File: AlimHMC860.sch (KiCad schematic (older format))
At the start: 21 parts, among them U2 HMC860LP3E

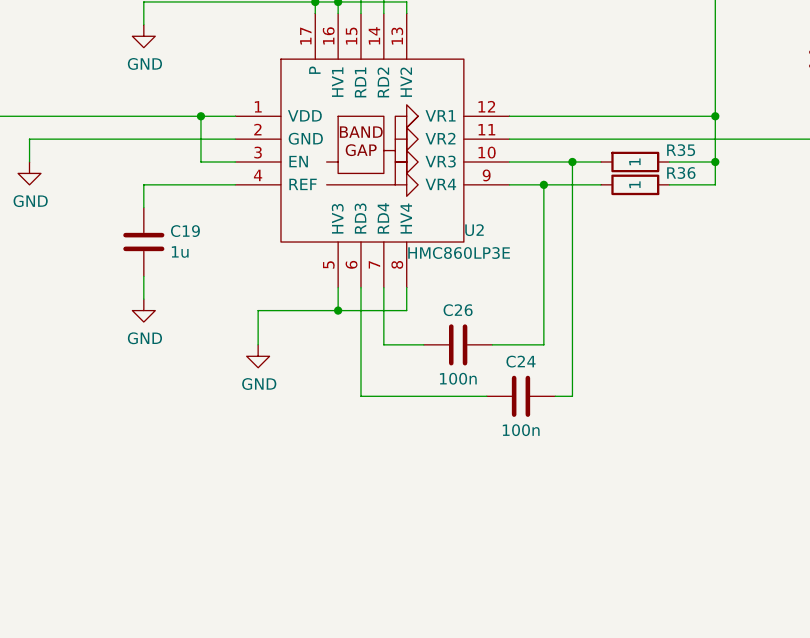
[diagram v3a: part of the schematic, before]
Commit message: added the option to switch HMC860 for HMC1060
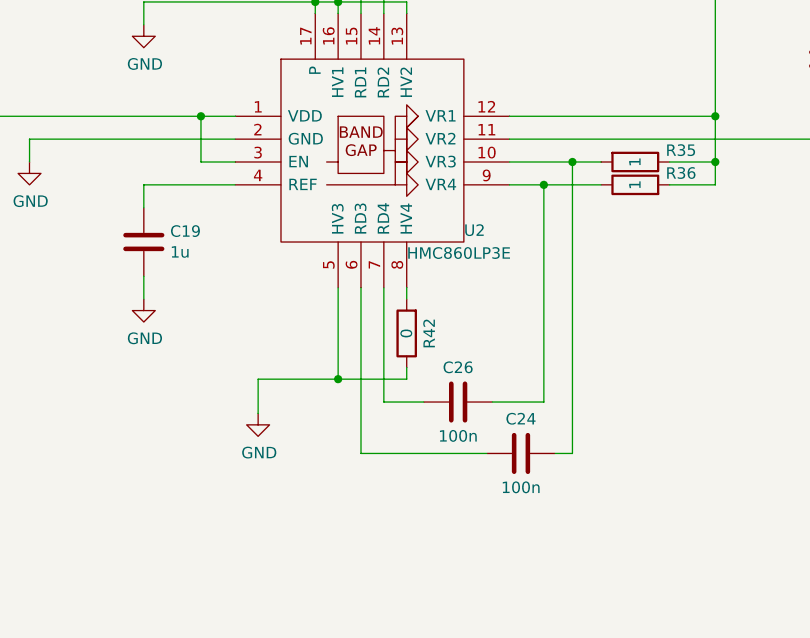
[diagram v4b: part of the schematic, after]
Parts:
- added R42: 0, Resistor_SMD:R_0603_1608Metric_Pad0.98x0.95mm_HandSolder, symbol Device:R
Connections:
- net GND: now also R42.1; no longer U2.8 (HV4)
- new net: R42.2, U2.8 (HV4)
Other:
- moved on the sheet: C24, C26
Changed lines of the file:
@@
 L Device:C C?
 U 1 1 618A0679
-P 5375 4000
+P 5375 4250
 AR Path="/618A0679" Ref="C?"  Part="1"
 AR Path="/6188E6DD/618A0679" Ref="C26"  Part="1"
-F 0 "C26" V 5225 4000 50  0000 C CNN
-F 1 "100n" V 5525 4000 50  0000 C CNN
-F 2 "Capacitor_SMD:C_0603_1608Metric_Pad1.08x0.95mm_HandSolder" H 5413 3850 50  0001 C CNN
-F 3 "~" H 5375 4000 50  0001 C CNN
-	1    5375 4000
-	0    1    1    0
-$EndComp
-Wire Wire Line
-	5525 4000 5750 4000
+F 0 "C26" V 5225 4250 50  0000 C CNN
+F 1 "100n" V 5525 4250 50  0000 C CNN
+F 2 "Capacitor_SMD:C_0603_1608Metric_Pad1.08x0.95mm_HandSolder" H 5413 4100 50  0001 C CNN
+F 3 "~" H 5375 4250 50  0001 C CNN
+	1    5375 4250
+	0    1    1    0
+$EndComp
+Wire Wire Line
+	5525 4250 5750 4250
 $Comp
 L Device:C C?
@@
 L Device:C C?
 U 1 1 618FCC1B
-P 5650 4225
+P 5650 4475
 AR Path="/618FCC1B" Ref="C?"  Part="1"
 AR Path="/6188E6DD/618FCC1B" Ref="C24"  Part="1"
-F 0 "C24" V 5500 4225 50  0000 C CNN
-F 1 "100n" V 5800 4225 50  0000 C CNN
-F 2 "Capacitor_SMD:C_0603_1608Metric_Pad1.08x0.95mm_HandSolder" H 5688 4075 50  0001 C CNN
-F 3 "~" H 5650 4225 50  0001 C CNN
-	1    5650 4225
+F 0 "C24" V 5500 4475 50  0000 C CNN
+F 1 "100n" V 5800 4475 50  0000 C CNN
+F 2 "Capacitor_SMD:C_0603_1608Metric_Pad1.08x0.95mm_HandSolder" H 5688 4325 50  0001 C CNN
+F 3 "~" H 5650 4475 50  0001 C CNN
+	1    5650 4475
 	0    1    1    0
 $EndComp
@@
 	8500 3900 8500 4000
 Wire Wire Line
-	5800 4225 5875 4225
+	5800 4475 5875 4475
 Wire Wire Line
 	9000 4500 7400 4500
@@
 	6500 3000 6500 3200
 Wire Wire Line
-	5050 4000 5050 3750
-Wire Wire Line
-	5050 4000 5225 4000
+	5050 4250 5050 3750
+Wire Wire Line
+	5050 4250 5225 4250
 Wire Wire Line
 	6000 3200 5875 3200
 Wire Wire Line
-	4950 3750 4950 4225
-Wire Wire Line
-	4950 4225 5500 4225
+	4950 3750 4950 4475
+Wire Wire Line
+	4950 4475 5500 4475
 Wire Wire Line
 	4950 2550 4950 2000
@@
 L power:GND #PWR0152
 U 1 1 619C6A8B
-P 4500 4000
-F 0 "#PWR0152" H 4500 3750 50  0001 C CNN
-F 1 "GND" H 4505 3827 50  0000 C CNN
-F 2 "" H 4500 4000 50  0001 C CNN
-F 3 "" H 4500 4000 50  0001 C CNN
-	1    4500 4000
-	1    0    0    -1
-$EndComp
-Wire Wire Line
-	4500 3850 4500 4000
-Wire Wire Line
-	5150 3850 5150 3750
-Wire Wire Line
-	4500 3850 4850 3850
-Wire Wire Line
-	4850 3750 4850 3850
-Connection ~ 4850 3850
-Wire Wire Line
-	4850 3850 5150 3850
+P 4500 4300
+F 0 "#PWR0152" H 4500 4050 50  0001 C CNN
+F 1 "GND" H 4505 4127 50  0000 C CNN
+F 2 "" H 4500 4300 50  0001 C CNN
+F 3 "" H 4500 4300 50  0001 C CNN
+	1    4500 4300
+	1    0    0    -1
+$EndComp
+Wire Wire Line
+	4500 4150 4500 4300
+Wire Wire Line
+	5150 4150 5150 4100
+Wire Wire Line
+	4500 4150 4850 4150
+Wire Wire Line
+	4850 3750 4850 4150
+Connection ~ 4850 4150
+Wire Wire Line
+	4850 4150 5150 4150
 Wire Wire Line
 	4400 3200 4250 3200
@@
 	9500 4500 9600 4500
 Wire Wire Line
-	5750 3300 5750 4000
+	5750 3300 5750 4250
 $Comp
 L Device:R R?
@@
 $EndComp
 Wire Wire Line
-	5875 4225 5875 3200
+	5875 4475 5875 3200
 Connection ~ 5875 3200
 Wire Wire Line
@@
 	0    -1   -1   0
 $EndComp
+$Comp
+L Device:R R?
+U 1 1 614CAA1C
+P 5150 3950
+AR Path="/614CAA1C" Ref="R?"  Part="1"
+AR Path="/6188E6DD/614CAA1C" Ref="R42"  Part="1"
+F 0 "R42" V 5050 3950 50  0000 C CNN
+F 1 "0" V 5150 3950 50  0000 C CNN
+F 2 "Resistor_SMD:R_0603_1608Metric_Pad0.98x0.95mm_HandSolder" V 5080 3950 50  0001 C CNN
+F 3 "~" H 5150 3950 50  0001 C CNN
+	1    5150 3950
+	-1   0    0    1
+$EndComp
+Wire Wire Line
+	5150 3800 5150 3750
 $EndSCHEMATC
